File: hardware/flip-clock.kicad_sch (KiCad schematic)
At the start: 9 parts, among them J1 Screw_Terminal_01x02, U1 ESP-01v090, U2 AP1117-33

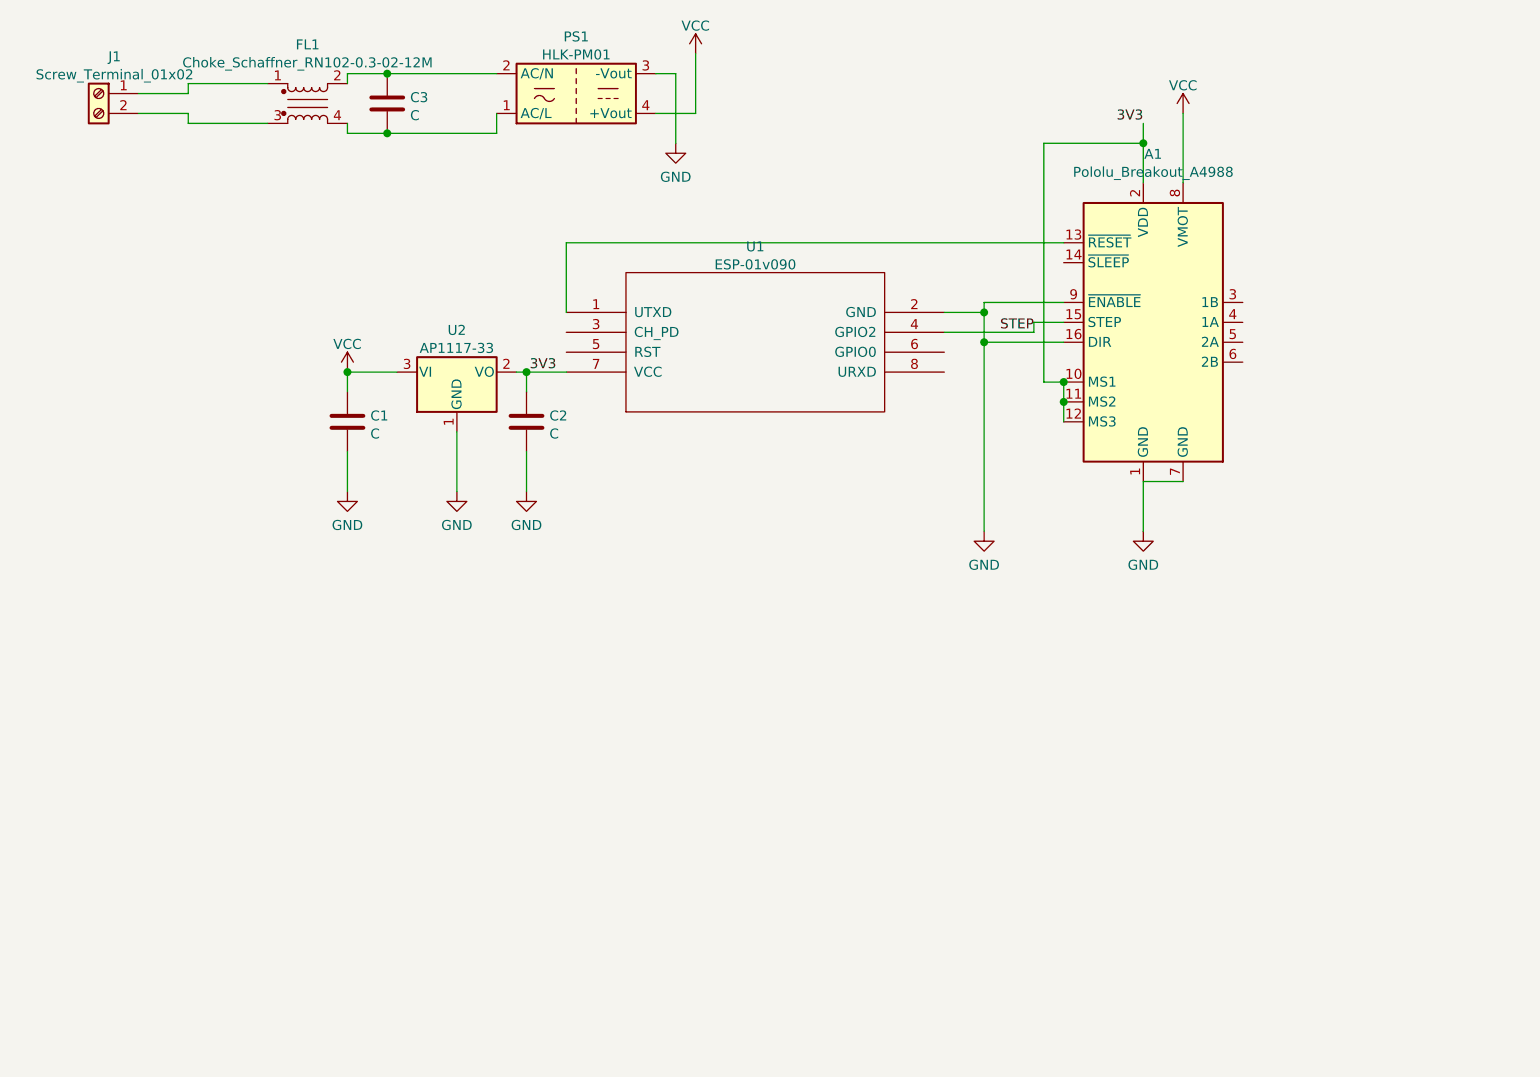
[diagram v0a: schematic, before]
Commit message: Layout without choke
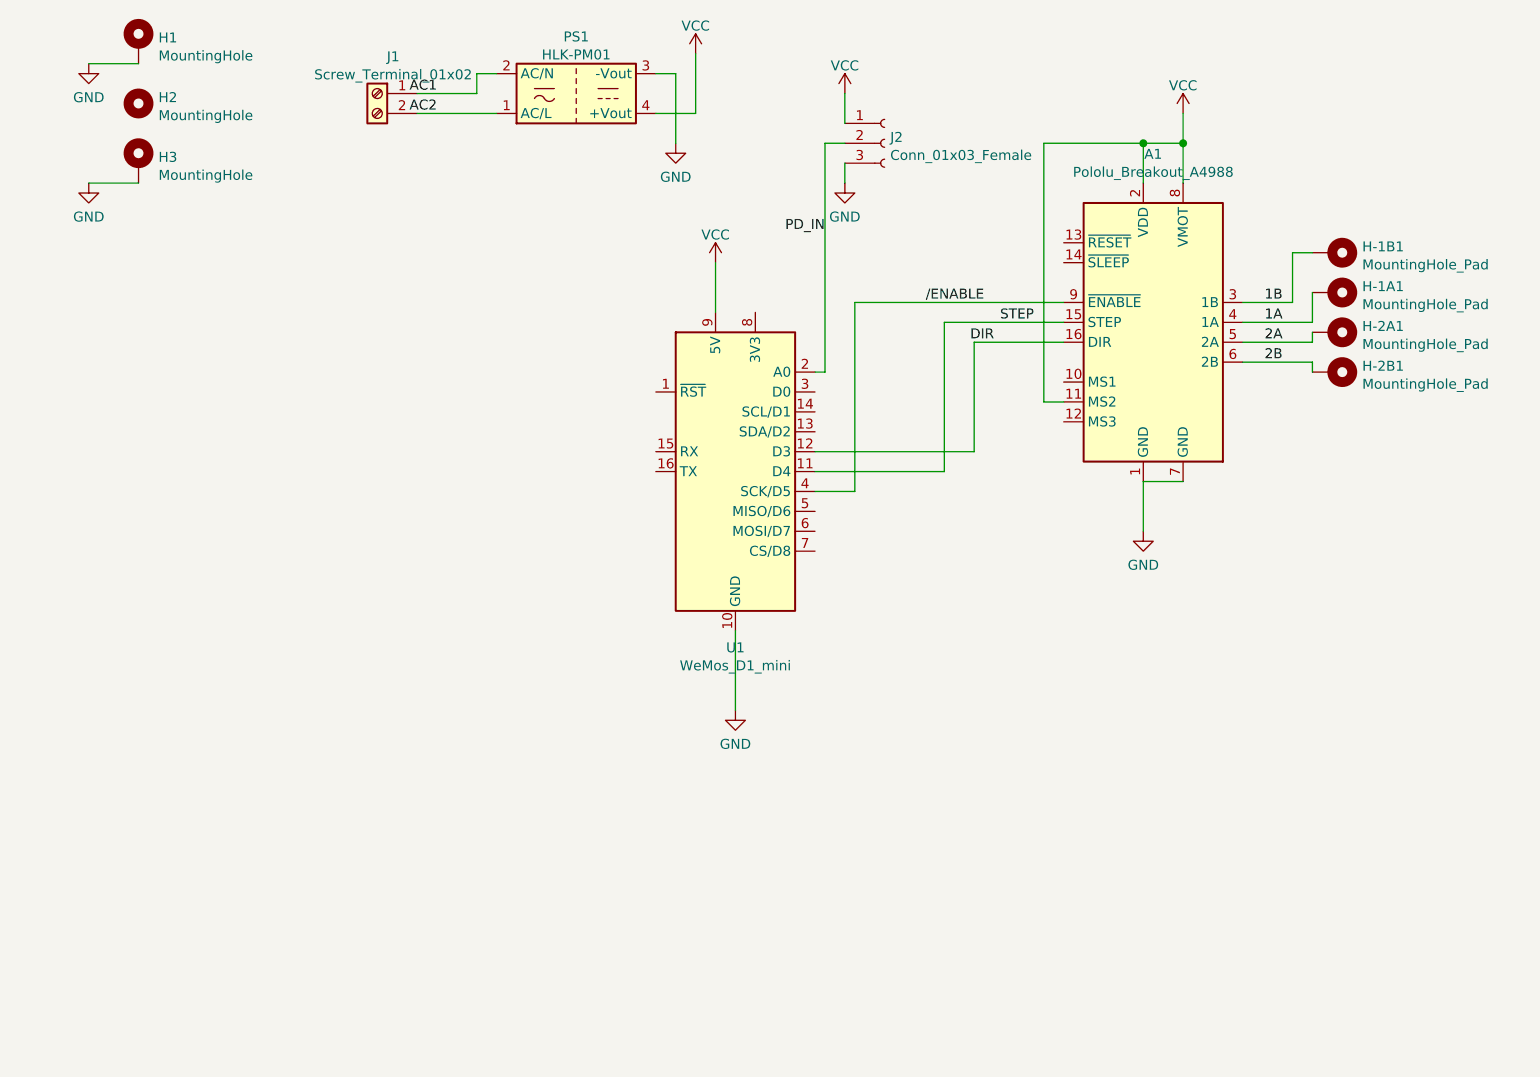
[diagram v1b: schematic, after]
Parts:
- removed C1, C2: C, Capacitor_SMD:C_0805_2012Metric, symbol Device:C
- removed C3: C, Capacitor_THT:C_Rect_L13.0mm_W6.0mm_P10.00mm_FKS3_FKP3_MKS4, symbol Device:C
- removed FL1: Choke_Schaffner_RN102-0.3-02-12M, Inductor_THT:Choke_Schaffner_RN102-04-14.0x14.0mm, symbol Filter:Choke_Schaffner_RN102-0.3-02-12M
- removed U1: ESP-01v090, ESP:ESP-01, symbol ESP:ESP-01v090
- removed U2: AP1117-33, Package_TO_SOT_SMD:SOT-223-3_TabPin2, symbol Regulator_Linear:AP1117-33
- added H-1A1, H-1B1, H-2A1, H-2B1: MountingHole_Pad, Connector_Wire:SolderWire-0.1sqmm_1x01_D0.4mm_OD1mm, symbol Mechanical:MountingHole_Pad
- added H1, H3: MountingHole, MountingHole:MountingHole_3.2mm_M3_Pad_Via, symbol Mechanical:MountingHole_Pad
- added H2: MountingHole, MountingHole:MountingHole_5.3mm_M5, symbol Mechanical:MountingHole
- added J2: Conn_01x03_Female, Connector:FanPinHeader_1x03_P2.54mm_Vertical, symbol Connector:Conn_01x03_Female
- added U1: WeMos_D1_mini, Module:WEMOS_D1_mini_light, symbol MCU_Module:WeMos_D1_mini
- PS1: footprint Converter_ACDC:Converter_ACDC_HiLink_HLK-2Mxx -> Converter_ACDC:Converter_ACDC_HiLink_HLK-PMxx
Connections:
- net GND: now also H1.1, H3.1, J2.3 (Pin_3), U1.10 (GND); no longer A1.16 (DIR), A1.9 (~ENABLE)
- net STEP: now also U1.11 (D4)
- net VCC: now also A1.11 (MS2), A1.2 (VDD), J2.1 (Pin_1), U1.9 (5V)
- net AC1: now reaches J1.1 (Pin_1)
- net AC1: now also PS1.2 (AC/N)
- net AC2: now reaches J1.2 (Pin_2)
- net AC2: now also PS1.1 (AC/L)
- net 1B: now reaches A1.3 (1B)
- net 1B: now also H-1B1.1
- net 1A: now reaches A1.4 (1A)
- net 1A: now also H-1A1.1
- net 2A: now reaches A1.5 (2A)
- net 2A: now also H-2A1.1
- net 2B: now reaches A1.6 (2B)
- net 2B: now also H-2B1.1
- removed net 3V3: A1.10 (MS1), A1.11 (MS2), A1.12 (MS3), A1.2 (VDD)
- new net DIR: A1.16 (DIR), U1.12 (D3)
- new net PD_IN: J2.2 (Pin_2), U1.2 (A0)
- new net /ENABLE: A1.9 (~ENABLE), U1.4 (SCK/D5)
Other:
- moved on the sheet: J1

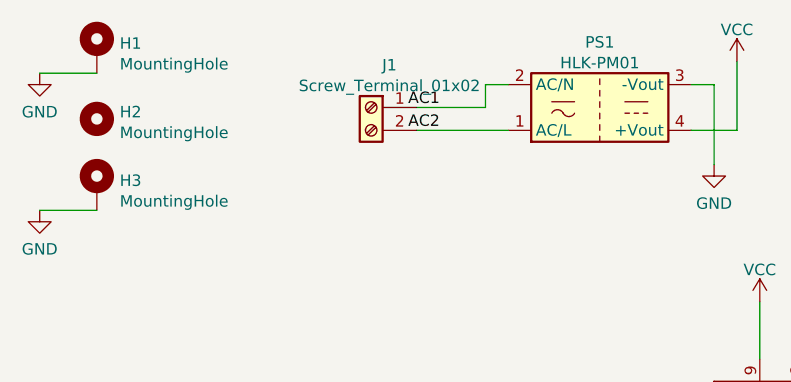
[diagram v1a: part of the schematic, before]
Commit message: Wrong side populated
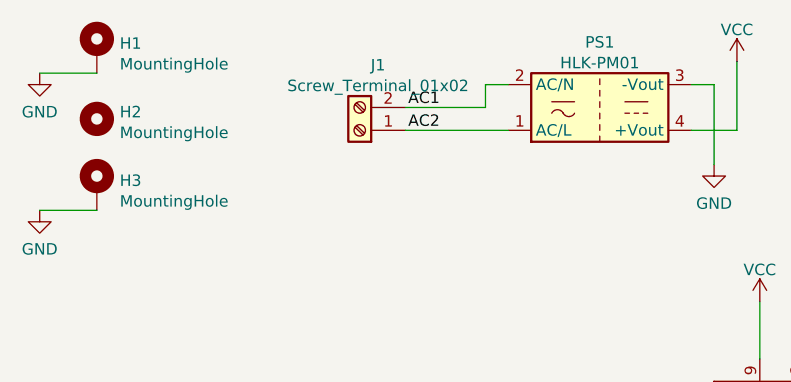
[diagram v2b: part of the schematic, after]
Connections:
- net AC1: now also J1.2 (Pin_2); no longer J1.1 (Pin_1)
- net AC2: now also J1.1 (Pin_1); no longer J1.2 (Pin_2)
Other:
- moved on the sheet: J1
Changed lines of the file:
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@@
     (stroke (width 0) (type solid) (color 0 0 0 0))
   )
-  (wire (pts (xy 63.5 29.21) (xy 71.12 29.21))
-    (stroke (width 0) (type solid) (color 0 0 0 0))
-  )
-  (wire (pts (xy 63.5 31.75) (xy 73.66 31.75))
+  (wire (pts (xy 62.23 29.21) (xy 71.12 29.21))
+    (stroke (width 0) (type solid) (color 0 0 0 0))
+  )
+  (wire (pts (xy 62.23 31.75) (xy 73.66 31.75))
     (stroke (width 0) (type solid) (color 0 0 0 0))
   )
@@
     (pin "3")
   )
-  (symbol (lib_id "Connector:Screw_Terminal_01x02") (at 58.42 29.21 0) (mirror y) (unit 1)
-    (in_bom yes) (on_board yes) (fields_autoplaced)
-    (property "Reference" "J1" (id 0) (at 60.452 24.5068 0))
-    (property "Value" "Screw_Terminal_01x02" (id 1) (at 60.452 26.8055 0))
-    (property "Footprint" "TerminalBlock_Phoenix:TerminalBlock_Phoenix_MKDS-1,5-2_1x02_P5.00mm_Horizontal" (id 2) (at 58.42 29.21 0)
-      (effects (font (size 1.27 1.27)) hide)
-    )
-    (property "Datasheet" "~" (id 3) (at 58.42 29.21 0)
-      (effects (font (size 1.27 1.27)) hide)
-    )
+  (symbol (lib_id "Connector:Screw_Terminal_01x02") (at 57.15 31.75 180) (unit 1)
+    (in_bom yes) (on_board yes) (fields_autoplaced)
+    (property "Reference" "J1" (id 0) (at 59.182 24.5068 0))
+    (property "Value" "Screw_Terminal_01x02" (id 1) (at 59.182 26.8055 0))
+    (property "Footprint" "TerminalBlock_Phoenix:TerminalBlock_Phoenix_MKDS-1,5-2_1x02_P5.00mm_Horizontal" (id 2) (at 57.15 31.75 0)
+      (effects (font (size 1.27 1.27)) hide)
+    )
+    (property "Datasheet" "~" (id 3) (at 57.15 31.75 0)
+      (effects (font (size 1.27 1.27)) hide)
+    )

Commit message: Correct side
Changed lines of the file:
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@@
     (stroke (width 0) (type solid) (color 0 0 0 0))
   )
-  (label "AC1" (at 66.04 29.21 180)
+  (label "AC2" (at 66.04 31.75 0)
+    (effects (font (size 1.27 1.27)) (justify left bottom))
+  )
+  (label "AC1" (at 69.85 29.21 180)
     (effects (font (size 1.27 1.27)) (justify right bottom))
   )
-  (label "AC2" (at 66.04 31.75 180)
-    (effects (font (size 1.27 1.27)) (justify right bottom))
-  )

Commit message: Pre-Production
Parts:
- removed J2: Conn_01x03_Female, Connector:FanPinHeader_1x03_P2.54mm_Vertical, symbol Connector:Conn_01x03_Female
- added J2: Conn_01x04, Connector_Wire:SolderWire-0.1sqmm_1x04_P3.6mm_D0.4mm_OD1mm, symbol Connector_Generic:Conn_01x04
- added R1: 4k7, Resistor_SMD:R_0805_2012Metric, symbol Device:R
- H1, H3: footprint MountingHole:MountingHole_3.2mm_M3_Pad_Via -> MountingHole:MountingHole_3.2mm_M3_Pad
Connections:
- net GND: now also J2.4 (Pin_4)
- net PD_IN: now also J2.2 (Pin_2)
- net VCC: now also J2.1 (Pin_1), R1.1
- net SDA: now reaches U1.13 (SDA/D2)
- net SCL: now reaches U1.14 (SCL/D1)
- net HOUR: now reaches U1.3 (D0)
- net HOUR: now also J2.3 (Pin_3), R1.2
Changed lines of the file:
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@@
 (kicad_sch (version 20210406) (generator eeschema)
   (paper "A4")
+  (junction (at 118.11 33.02) (diameter 0.9144) (color 0 0 0 0))
+  (junction (at 118.11 40.64) (diameter 0.9144) (color 0 0 0 0))
   (junction (at 156.21 35.56) (diameter 1.016) (color 0 0 0 0))
   (junction (at 161.29 35.56) (diameter 1.016) (color 0 0 0 0))
@@
     (stroke (width 0) (type solid) (color 0 0 0 0))
   )
+  (wire (pts (xy 110.49 33.02) (xy 118.11 33.02))
+    (stroke (width 0) (type solid) (color 0 0 0 0))
+  )
+  (wire (pts (xy 110.49 40.64) (xy 118.11 40.64))
+    (stroke (width 0) (type solid) (color 0 0 0 0))
+  )
+  (wire (pts (xy 114.3 67.31) (xy 118.11 67.31))
+    (stroke (width 0) (type solid) (color 0 0 0 0))
+  )
+  (wire (pts (xy 114.3 69.85) (xy 118.11 69.85))
+    (stroke (width 0) (type solid) (color 0 0 0 0))
+  )
+  (wire (pts (xy 114.3 72.39) (xy 118.11 72.39))
+    (stroke (width 0) (type solid) (color 0 0 0 0))
+  )
   (wire (pts (xy 114.3 74.93) (xy 134.62 74.93))
     (stroke (width 0) (type solid) (color 0 0 0 0))
@@
     (stroke (width 0) (type solid) (color 0 0 0 0))
   )
+  (wire (pts (xy 115.57 35.56) (xy 123.19 35.56))
+    (stroke (width 0) (type solid) (color 0 0 0 0))
+  )
   (wire (pts (xy 115.57 64.77) (xy 114.3 64.77))
     (stroke (width 0) (type solid) (color 0 0 0 0))
@@
     (stroke (width 0) (type solid) (color 0 0 0 0))
   )
-  (wire (pts (xy 118.11 35.56) (xy 115.57 35.56))
-    (stroke (width 0) (type solid) (color 0 0 0 0))
-  )
-  (wire (pts (xy 118.11 38.1) (xy 118.11 40.64))
+  (wire (pts (xy 118.11 33.02) (xy 123.19 33.02))
+    (stroke (width 0) (type solid) (color 0 0 0 0))
+  )
+  (wire (pts (xy 118.11 38.1) (xy 123.19 38.1))
+    (stroke (width 0) (type solid) (color 0 0 0 0))
+  )
+  (wire (pts (xy 118.11 40.64) (xy 118.11 38.1))
+    (stroke (width 0) (type solid) (color 0 0 0 0))
+  )
+  (wire (pts (xy 118.11 67.31) (xy 118.11 40.64))
     (stroke (width 0) (type solid) (color 0 0 0 0))
   )
@@
   )
   (wire (pts (xy 119.38 80.01) (xy 114.3 80.01))
+    (stroke (width 0) (type solid) (color 0 0 0 0))
+  )
+  (wire (pts (xy 120.65 40.64) (xy 120.65 44.45))
+    (stroke (width 0) (type solid) (color 0 0 0 0))
+  )
+  (wire (pts (xy 120.65 40.64) (xy 123.19 40.64))
     (stroke (width 0) (type solid) (color 0 0 0 0))
   )
@@
     (effects (font (size 1.27 1.27)) (justify right bottom))
   )
+  (label "HOUR" (at 118.11 49.53 180)
+    (effects (font (size 1.27 1.27)) (justify right bottom))
+  )
+  (label "SCL" (at 118.11 69.85 180)
+    (effects (font (size 1.27 1.27)) (justify right bottom))
+  )
+  (label "SDA" (at 118.11 72.39 180)
+    (effects (font (size 1.27 1.27)) (justify right bottom))
+  )
   (label "{slash}ENABLE" (at 135.89 55.88 180)
     (effects (font (size 1.27 1.27)) (justify right bottom))
@@
     (pin "1")
   )
-  (symbol (lib_id "power:GND") (at 118.11 40.64 0) (unit 1)
-    (in_bom yes) (on_board yes) (fields_autoplaced)
-    (property "Reference" "#PWR05" (id 0) (at 118.11 46.99 0)
-      (effects (font (size 1.27 1.27)) hide)
-    )
-    (property "Value" "GND" (id 1) (at 118.11 44.9644 0))
-    (property "Footprint" "" (id 2) (at 118.11 40.64 0)
-      (effects (font (size 1.27 1.27)) hide)
-    )
-    (property "Datasheet" "" (id 3) (at 118.11 40.64 0)
+  (symbol (lib_id "power:GND") (at 120.65 44.45 0) (unit 1)
+    (in_bom yes) (on_board yes) (fields_autoplaced)
+    (property "Reference" "#PWR05" (id 0) (at 120.65 50.8 0)
+      (effects (font (size 1.27 1.27)) hide)
+    )
+    (property "Value" "GND" (id 1) (at 120.65 48.7744 0))
+    (property "Footprint" "" (id 2) (at 120.65 44.45 0)
+      (effects (font (size 1.27 1.27)) hide)
+    )
+    (property "Datasheet" "" (id 3) (at 120.65 44.45 0)
       (effects (font (size 1.27 1.27)) hide)
     )
@@
     )
   )
+  (symbol (lib_id "Device:R") (at 110.49 36.83 0) (unit 1)
+    (in_bom yes) (on_board yes) (fields_autoplaced)
+    (property "Reference" "R1" (id 0) (at 112.2681 36.0691 0)
+      (effects (font (size 1.27 1.27)) (justify left))
+    )
+    (property "Value" "4k7" (id 1) (at 112.2681 38.3678 0)
+      (effects (font (size 1.27 1.27)) (justify left))
+    )
+    (property "Footprint" "Resistor_SMD:R_0805_2012Metric" (id 2) (at 108.712 36.83 90)
+      (effects (font (size 1.27 1.27)) hide)
+    )
+    (property "Datasheet" "~" (id 3) (at 110.49 36.83 0)
+      (effects (font (size 1.27 1.27)) hide)
+    )
+    (pin "1")
+    (pin "2")
+  )
   (symbol (lib_id "Mechanical:MountingHole_Pad") (at 27.94 22.86 0) (unit 1)
     (in_bom yes) (on_board yes) (fields_autoplaced)
@@
       (effects (font (size 1.27 1.27)) (justify left))
     )
-    (property "Footprint" "MountingHole:MountingHole_3.2mm_M3_Pad_Via" (id 2) (at 27.94 22.86 0)
+    (property "Footprint" "MountingHole:MountingHole_3.2mm_M3_Pad" (id 2) (at 27.94 22.86 0)
       (effects (font (size 1.27 1.27)) hide)
     )
@@
       (effects (font (size 1.27 1.27)) (justify left))
     )
-    (property "Footprint" "MountingHole:MountingHole_3.2mm_M3_Pad_Via" (id 2) (at 27.94 38.1 0)
+    (property "Footprint" "MountingHole:MountingHole_3.2mm_M3_Pad" (id 2) (at 27.94 38.1 0)
       (effects (font (size 1.27 1.27)) hide)
     )
@@
     )
     (pin "1")
-  )
-  (symbol (lib_id "Connector:Conn_01x03_Female") (at 123.19 35.56 0) (unit 1)
-    (in_bom yes) (on_board yes) (fields_autoplaced)
-    (property "Reference" "J2" (id 0) (at 123.9013 34.7991 0)
-      (effects (font (size 1.27 1.27)) (justify left))
-    )
-    (property "Value" "Conn_01x03_Female" (id 1) (at 123.9013 37.0978 0)
-      (effects (font (size 1.27 1.27)) (justify left))
-    )
-    (property "Footprint" "Connector:FanPinHeader_1x03_P2.54mm_Vertical" (id 2) (at 123.19 35.56 0)
-      (effects (font (size 1.27 1.27)) hide)
-    )
-    (property "Datasheet" "~" (id 3) (at 123.19 35.56 0)
-      (effects (font (size 1.27 1.27)) hide)
-    )
-    (pin "1")
-    (pin "2")
-    (pin "3")
   )
   (symbol (lib_id "Connector:Screw_Terminal_01x02") (at 57.15 31.75 180) (unit 1)
@@
     (pin "1")
     (pin "2")
+  )
+  (symbol (lib_id "Connector_Generic:Conn_01x04") (at 128.27 35.56 0) (unit 1)
+    (in_bom yes) (on_board yes) (fields_autoplaced)
+    (property "Reference" "J2" (id 0) (at 130.3021 36.0691 0)
+      (effects (font (size 1.27 1.27)) (justify left))
+    )
+    (property "Value" "Conn_01x04" (id 1) (at 130.3021 38.3678 0)
+      (effects (font (size 1.27 1.27)) (justify left))
+    )
+    (property "Footprint" "Connector_Wire:SolderWire-0.1sqmm_1x04_P3.6mm_D0.4mm_OD1mm" (id 2) (at 128.27 35.56 0)
+      (effects (font (size 1.27 1.27)) hide)
+    )
+    (property "Datasheet" "~" (id 3) (at 128.27 35.56 0)
+      (effects (font (size 1.27 1.27)) hide)
+    )
+    (pin "1")
+    (pin "2")
+    (pin "3")
+    (pin "4")
   )
   (symbol (lib_id "Converter_ACDC:HLK-PM01") (at 83.82 29.21 0) (mirror x) (unit 1)
@@
     )
     (path "/fcb6db2a-6ac4-4826-8d03-7182be766e68"
-      (reference "H1") (unit 1) (value "MountingHole") (footprint "MountingHole:MountingHole_3.2mm_M3_Pad_Via")
+      (reference "H1") (unit 1) (value "MountingHole") (footprint "MountingHole:MountingHole_3.2mm_M3_Pad")
     )
     (path "/bd3b6799-2eb4-4368-9c1b-cb20f1e606db"
@@
     )
     (path "/0758d31c-a98c-4212-8b72-59b9e1d10664"
-      (reference "H3") (unit 1) (value "MountingHole") (footprint "MountingHole:MountingHole_3.2mm_M3_Pad_Via")
+      (reference "H3") (unit 1) (value "MountingHole") (footprint "MountingHole:MountingHole_3.2mm_M3_Pad")
     )
     (path "/f713f965-e52a-49ca-82fb-31c7d4eb52c8"
@@
       (reference "J1") (unit 1) (value "Screw_Terminal_01x02") (footprint "TerminalBlock_Phoenix:TerminalBlock_Phoenix_MKDS-1,5-2_1x02_P5.00mm_Horizontal")
     )
-    (path "/fcfbe08d-0417-4528-a18b-a9c5976c2554"
-      (reference "J2") (unit 1) (value "Conn_01x03_Female") (footprint "Connector:FanPinHeader_1x03_P2.54mm_Vertical")
+    (path "/9f064d7b-2865-4666-8023-e90006907a35"
+      (reference "J2") (unit 1) (value "Conn_01x04") (footprint "Connector_Wire:SolderWire-0.1sqmm_1x04_P3.6mm_D0.4mm_OD1mm")
     )
     (path "/b4e9ba94-1e48-4e68-ad99-460f09cc50a2"
       (reference "PS1") (unit 1) (value "HLK-PM01") (footprint "Converter_ACDC:Converter_ACDC_HiLink_HLK-PMxx")
     )
+    (path "/58bce13c-d699-4461-a4ab-97430eb06ca1"
+      (reference "R1") (unit 1) (value "4k7") (footprint "Resistor_SMD:R_0805_2012Metric")
+    )
     (path "/967d53ac-169d-48b6-a5fc-633424bf7271"

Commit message: JST Connector for IR and hour
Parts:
- J2: footprint Connector_Wire:SolderWire-0.1sqmm_1x04_P3.6mm_D0.4mm_OD1mm -> Connector_JST:JST_PH_B4B-PH-K_1x04_P2.00mm_Vertical
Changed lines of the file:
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@@
       (effects (font (size 1.27 1.27)) (justify left))
     )
-    (property "Footprint" "Connector_Wire:SolderWire-0.1sqmm_1x04_P3.6mm_D0.4mm_OD1mm" (id 2) (at 128.27 35.56 0)
+    (property "Footprint" "Connector_JST:JST_PH_B4B-PH-K_1x04_P2.00mm_Vertical" (id 2) (at 128.27 35.56 0)
       (effects (font (size 1.27 1.27)) hide)
     )
@@
     )
     (path "/9f064d7b-2865-4666-8023-e90006907a35"
-      (reference "J2") (unit 1) (value "Conn_01x04") (footprint "Connector_Wire:SolderWire-0.1sqmm_1x04_P3.6mm_D0.4mm_OD1mm")
+      (reference "J2") (unit 1) (value "Conn_01x04") (footprint "Connector_JST:JST_PH_B4B-PH-K_1x04_P2.00mm_Vertical")
     )
     (path "/b4e9ba94-1e48-4e68-ad99-460f09cc50a2"
